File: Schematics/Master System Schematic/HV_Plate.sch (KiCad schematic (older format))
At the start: 14 parts, among them K1 AIR-: GX14, K53 PCharge: P105BDA, K54 AIR+: GX14, K55 DCharge: PNC113, U5 OrionCurrentSens

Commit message: LV Plate
> Added basic connectors and outlines for MCR PCB
> Added and wired components on LV Plate
> Added GLV connector
> Connected layers
> Some wire gauges still needed

LV_Plate Version 1.0
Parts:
- U5: symbol Master-System-Schematic-rescue:OrionCurrentSens-NER -> NER:OrionCurrentSens
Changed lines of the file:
@@
 $Descr A 11000 8500
 encoding utf-8
-Sheet 27 38
+Sheet 20 40
 Title "HV Plate"
 Date "2021-04-15"
@@
 $EndComp
 $Comp
-L Master-System-Schematic-rescue:OrionCurrentSens-NER U?
+L NER:OrionCurrentSens U?
 U 1 1 6082A419
 P 7400 5250

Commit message: Master Cleanup
> BattBox sheet tweaks
> Removed IMD container
> Removed BattBox fans from master
> Removed BMS container, temporarily moved VPM sheet
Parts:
- renumbered F204 to F?, F203 to F?, F205 to F?, F201 to F?, F202 to F?, K1 to K?, K53 to K?, K54 to K?, K55 to K?, R13 to R?, R16 to R?, R12 to R?, R11 to R?
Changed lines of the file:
@@
 $Descr A 11000 8500
 encoding utf-8
-Sheet 7 27
+Sheet 7 25
 Title "HV Plate"
 Date "2021-04-15"
@@
 $EndDescr
 $Comp
-L Device:R R11
+L Device:R R?
 U 1 1 608CF874
 P 6150 3350
-F 0 "R11" H 5750 3450 50  0000 C CNN
+F 0 "R?" H 5750 3450 50  0000 C CNN
 F 1 "PCharge: 600R" H 5750 3350 50  0000 C CNN
 F 2 "" V 6080 3350 50  0001 C CNN
@@
 $EndComp
 $Comp
-L Relay:DIPxx-1Axx-11x K1
+L Relay:DIPxx-1Axx-11x K?
 U 1 1 608D0328
 P 3450 5750
-F 0 "K1" V 2883 5750 50  0000 C CNN
+F 0 "K?" V 2883 5750 50  0000 C CNN
 F 1 "AIR-: GX14" V 2974 5750 50  0000 C CNN
 F 2 "Relay_THT:Relay_StandexMeder_DIP_LowProfile" H 3800 5700 50  0001 L CNN
@@
 $EndComp
 $Comp
-L Relay:DIPxx-1Axx-11x K54
+L Relay:DIPxx-1Axx-11x K?
 U 1 1 608D24D5
 P 4650 3750
-F 0 "K54" V 4083 3750 50  0000 C CNN
+F 0 "K?" V 4083 3750 50  0000 C CNN
 F 1 "AIR+: GX14" V 4174 3750 50  0000 C CNN
 F 2 "Relay_THT:Relay_StandexMeder_DIP_LowProfile" H 5000 3700 50  0001 L CNN
@@
 $EndComp
 $Comp
-L Device:Fuse F203
+L Device:Fuse F?
 U 1 1 608D366E
 P 2400 3950
-F 0 "F203" V 2203 3950 50  0000 C CNN
+F 0 "F?" V 2203 3950 50  0000 C CNN
 F 1 "TS Fuse: 200A" V 2294 3950 50  0000 C CNN
 F 2 "" V 2330 3950 50  0001 C CNN
@@
 $EndComp
 $Comp
-L Device:R R12
+L Device:R R?
 U 1 1 608CEF02
 P 7000 4450
-F 0 "R12" H 6650 4550 50  0000 C CNN
+F 0 "R?" H 6650 4550 50  0000 C CNN
 F 1 "DCharge: 3.3K" H 6650 4450 50  0000 C CNN
 F 2 "" V 6930 4450 50  0001 C CNN
@@
 $EndComp
 $Comp
-L Relay:MSxx-1Bxx-75 K55
+L Relay:MSxx-1Bxx-75 K?
 U 1 1 608D570D
 P 5600 5000
-F 0 "K55" V 5033 5000 50  0000 C CNN
+F 0 "K?" V 5033 5000 50  0000 C CNN
 F 1 "DCharge: PNC113" V 5124 5000 50  0000 C CNN
 F 2 "Relay_THT:Relay_SPST_StandexMeder_MS_Form1AB" H 5950 4950 50  0001 L CNN
@@
 $EndComp
 $Comp
-L Device:R R13
+L Device:R R?
 U 1 1 60827E73
 P 8950 3500
-F 0 "R13" H 8880 3454 50  0000 R CNN
+F 0 "R?" H 8880 3454 50  0000 R CNN
 F 1 "TSMP+: 10K" H 8880 3545 50  0000 R CNN
 F 2 "" V 8880 3500 50  0001 C CNN
@@
 $EndComp
 $Comp
-L Device:R R16
+L Device:R R?
 U 1 1 608282DF
 P 9050 3500
-F 0 "R16" H 8980 3454 50  0000 R CNN
+F 0 "R?" H 8980 3454 50  0000 R CNN
 F 1 "TSMP-: 10K" H 8980 3545 50  0000 R CNN
 F 2 "" V 8980 3500 50  0001 C CNN
@@
 AR Path="/5F45B05E/6082A419" Ref="U?"  Part="1"
 AR Path="/5F45B05E/6082840F/6082A419" Ref="U5"  Part="1"
-F 0 "U5" V 6950 4700 50  0000 C CNN
+F 0 "U?" V 6950 4700 50  0000 C CNN
 F 1 "OrionCurrentSens" V 6850 4700 50  0000 C CNN
 F 2 "" H 7400 5250 50  0001 C CNN
@@
 	7950 2450 7950 2800
 $Comp
-L Device:Fuse F204
+L Device:Fuse F?
 U 1 1 608289D7
 P 7850 2950
-F 0 "F204" H 7650 3050 50  0000 C CNN
+F 0 "F?" H 7650 3050 50  0000 C CNN
 F 1 "IMD Fuse+: 0.5A" H 7450 2950 50  0000 C CNN
 F 2 "" V 7780 2950 50  0001 C CNN
@@
 $EndComp
 $Comp
-L Device:Fuse F205
+L Device:Fuse F?
 U 1 1 608D8D1E
 P 7950 2950
-F 0 "F205" H 7750 3050 50  0000 C CNN
+F 0 "F?" H 7750 3050 50  0000 C CNN
 F 1 "IMD Fuse-: 0.5A" H 7550 2950 50  0000 C CNN
 F 2 "" V 7880 2950 50  0001 C CNN
@@
 PCharge_SigL
 $Comp
-L Relay:DIPxx-1Axx-11x K53
+L Relay:DIPxx-1Axx-11x K?
 U 1 1 608D1508
 P 4650 2650
-F 0 "K53" V 4083 2650 50  0000 C CNN
+F 0 "K?" V 4083 2650 50  0000 C CNN
 F 1 "PCharge: P105BDA" V 4174 2650 50  0000 C CNN
 F 2 "Relay_THT:Relay_StandexMeder_DIP_LowProfile" H 5000 2600 50  0001 L CNN
@@
 2x ??AWG
 $Comp
-L Device:Fuse F202
+L Device:Fuse F?
 U 1 1 6091E6DC
 P 1850 2950
-F 0 "F202" H 1700 3050 50  0000 C CNN
+F 0 "F?" H 1700 3050 50  0000 C CNN
 F 1 "TSAL Fuse-: ??A" H 1450 2950 50  0000 C CNN
 F 2 "" V 1780 2950 50  0001 C CNN
@@
 $EndComp
 $Comp
-L Device:Fuse F201
+L Device:Fuse F?
 U 1 1 6091E6D6
 P 1750 2950
-F 0 "F201" H 1600 3050 50  0000 C CNN
+F 0 "F?" H 1600 3050 50  0000 C CNN
 F 1 "TSAL Fuse+: ??A" H 1350 2950 50  0000 C CNN
 F 2 "" V 1680 2950 50  0001 C CNN

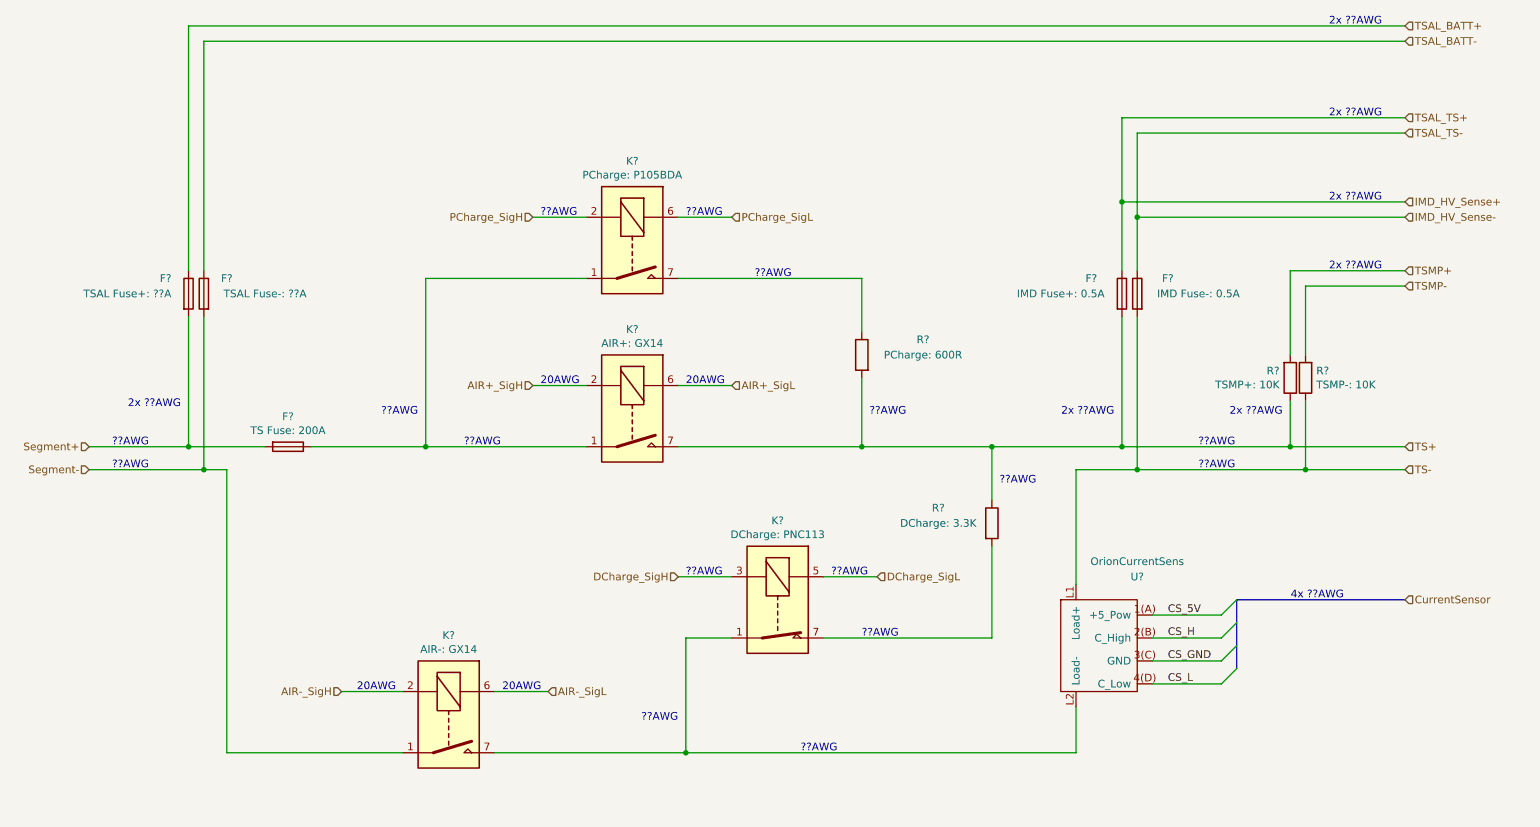
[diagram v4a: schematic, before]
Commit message: Battery Box KiCAD Update (#103)
* LV Plate and VPM board

Verified and updated LV plate connections
Setup VPM board stand-in
Organized main battery box schematic

* Battbox and master update

- Fixed all connections within battbox and did some formatting
- Added all battbox connections to master

* Annotations complete

* VPM callout

Added call to view altium schematic for VPM boarrd

* TSAL call out

Redirect to altium for TSAL

* Dates and stuff

- Final annotations
- Updated title blocks

* Exported

Plotted full file

Co-authored-by: Zack Perry <zperry2002@gmail.com>
Co-authored-by: Zack Perry <60787475+ziptol@users.noreply.github.com>
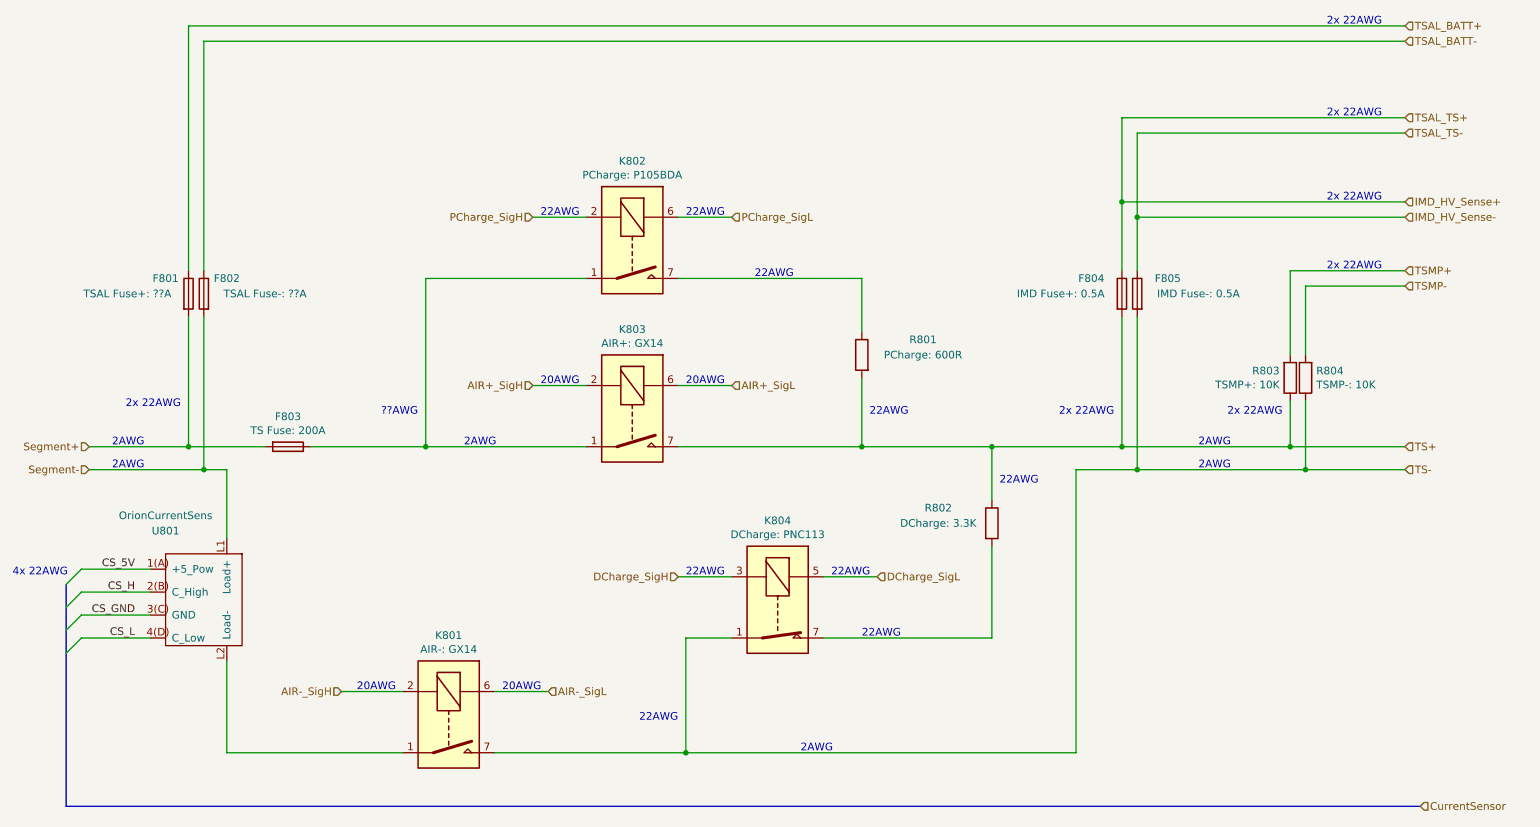
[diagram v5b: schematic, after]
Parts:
- gave numbers to parts that had none: 13
- renumbered U5 to U801
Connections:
- net Segment-: now also U801.L1 (Load+); no longer K801.1, K801.14
- net TS-: now also K801.7, K801.8, K804.1; no longer U801.L1 (Load+)
- new net: K801.1, K801.14, U801.L2 (Load-)
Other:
- note added: "22AWG"
- note added: "2AWG"
- note added: "2x 22AWG"
- note added: "4x 22AWG"
- note removed: "2x ??AWG"
- note removed: "4x ??AWG"
- moved on the sheet: U801
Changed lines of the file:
@@
 EESchema Schematic File Version 4
+LIBS:Master System Schematic-cache
 EELAYER 30 0
 EELAYER END
 $Descr A 11000 8500
 encoding utf-8
-Sheet 7 25
+Sheet 8 24
 Title "HV Plate"
 Date "2021-04-15"
 Rev "1.0"
-Comp ""
-Comment1 ""
-Comment2 ""
+Comp "Northeastern Electric Racing"
+Comment1 "https://github.com/Northeastern-Electric-Racing/NER"
+Comment2 "For authors and other info, contact Chief Electrical Engineer"
 Comment3 ""
 Comment4 ""
 $EndDescr
 $Comp
-L Device:R R?
+L Device:R R801
 U 1 1 608CF874
 P 6150 3350
-F 0 "R?" H 5750 3450 50  0000 C CNN
+F 0 "R801" H 5750 3450 50  0000 C CNN
 F 1 "PCharge: 600R" H 5750 3350 50  0000 C CNN
 F 2 "" V 6080 3350 50  0001 C CNN
@@
 $EndComp
 $Comp
-L Relay:DIPxx-1Axx-11x K?
+L Relay:DIPxx-1Axx-11x K801
 U 1 1 608D0328
 P 3450 5750
-F 0 "K?" V 2883 5750 50  0000 C CNN
+F 0 "K801" V 2883 5750 50  0000 C CNN
 F 1 "AIR-: GX14" V 2974 5750 50  0000 C CNN
 F 2 "Relay_THT:Relay_StandexMeder_DIP_LowProfile" H 3800 5700 50  0001 L CNN
@@
 $EndComp
 $Comp
-L Relay:DIPxx-1Axx-11x K?
+L Relay:DIPxx-1Axx-11x K803
 U 1 1 608D24D5
 P 4650 3750
-F 0 "K?" V 4083 3750 50  0000 C CNN
+F 0 "K803" V 4083 3750 50  0000 C CNN
 F 1 "AIR+: GX14" V 4174 3750 50  0000 C CNN
 F 2 "Relay_THT:Relay_StandexMeder_DIP_LowProfile" H 5000 3700 50  0001 L CNN
@@
 $EndComp
 $Comp
-L Device:Fuse F?
+L Device:Fuse F803
 U 1 1 608D366E
 P 2400 3950
-F 0 "F?" V 2203 3950 50  0000 C CNN
+F 0 "F803" V 2203 3950 50  0000 C CNN
 F 1 "TS Fuse: 200A" V 2294 3950 50  0000 C CNN
 F 2 "" V 2330 3950 50  0001 C CNN
@@
 $EndComp
 $Comp
-L Device:R R?
+L Device:R R802
 U 1 1 608CEF02
 P 7000 4450
-F 0 "R?" H 6650 4550 50  0000 C CNN
+F 0 "R802" H 6650 4550 50  0000 C CNN
 F 1 "DCharge: 3.3K" H 6650 4450 50  0000 C CNN
 F 2 "" V 6930 4450 50  0001 C CNN
@@
 $EndComp
 $Comp
-L Relay:MSxx-1Bxx-75 K?
+L Relay:MSxx-1Bxx-75 K804
 U 1 1 608D570D
 P 5600 5000
-F 0 "K?" V 5033 5000 50  0000 C CNN
+F 0 "K804" V 5033 5000 50  0000 C CNN
 F 1 "DCharge: PNC113" V 5124 5000 50  0000 C CNN
 F 2 "Relay_THT:Relay_SPST_StandexMeder_MS_Form1AB" H 5950 4950 50  0001 L CNN
@@
 $EndComp
 $Comp
-L Device:R R?
+L Device:R R803
 U 1 1 60827E73
 P 8950 3500
-F 0 "R?" H 8880 3454 50  0000 R CNN
+F 0 "R803" H 8880 3454 50  0000 R CNN
 F 1 "TSMP+: 10K" H 8880 3545 50  0000 R CNN
 F 2 "" V 8880 3500 50  0001 C CNN
@@
 $EndComp
 $Comp
-L Device:R R?
+L Device:R R804
 U 1 1 608282DF
 P 9050 3500
-F 0 "R?" H 8980 3454 50  0000 R CNN
+F 0 "R804" H 8980 3454 50  0000 R CNN
 F 1 "TSMP-: 10K" H 8980 3545 50  0000 R CNN
 F 2 "" V 8980 3500 50  0001 C CNN
@@
 L NER:OrionCurrentSens U?
 U 1 1 6082A419
-P 7400 5250
+P 2150 4950
 AR Path="/5F45B05E/6082A419" Ref="U?"  Part="1"
-AR Path="/5F45B05E/6082840F/6082A419" Ref="U5"  Part="1"
-F 0 "U?" V 6950 4700 50  0000 C CNN
-F 1 "OrionCurrentSens" V 6850 4700 50  0000 C CNN
-F 2 "" H 7400 5250 50  0001 C CNN
-F 3 "" H 7400 5250 50  0001 C CNN
-	1    7400 5250
-	0    -1   1    0
-$EndComp
-Text HLabel 9700 4950 2    50   Input ~ 0
+AR Path="/5F45B05E/6082840F/6082A419" Ref="U?"  Part="1"
+AR Path="/60C39CCE/6082840F/6082A419" Ref="U801"  Part="1"
+F 0 "U801" V 1700 4400 50  0000 C CNN
+F 1 "OrionCurrentSens" V 1600 4400 50  0000 C CNN
+F 2 "" H 2150 4950 50  0001 C CNN
+F 3 "" H 2150 4950 50  0001 C CNN
+	1    2150 4950
+	0    1    1    0
+$EndComp
+Text HLabel 9800 6300 2    50   Input ~ 0
 CurrentSensor
 Text HLabel 9700 3950 2    50   Input ~ 0
@@
 Segment-
 Entry Wire Line
-	8600 4950 8500 5050
+	1050 4750 950  4850
 Entry Wire Line
-	8600 5100 8500 5200
+	1050 4900 950  5000
 Entry Wire Line
-	8600 5250 8500 5350
+	1050 5050 950  5150
 Entry Wire Line
-	8600 5400 8500 5500
-Wire Wire Line
-	8500 5050 8050 5050
-Wire Wire Line
-	8500 5200 8050 5200
-Wire Wire Line
-	8500 5350 8050 5350
-Wire Wire Line
-	8500 5500 8050 5500
-Text Label 8150 5050 0    50   ~ 0
+	1050 5200 950  5300
+Wire Wire Line
+	1050 4750 1500 4750
+Wire Wire Line
+	1050 4900 1500 4900
+Wire Wire Line
+	1050 5050 1500 5050
+Wire Wire Line
+	1050 5200 1500 5200
+Text Label 1400 4750 2    50   ~ 0
 CS_5V
-Text Label 8150 5200 0    50   ~ 0
+Text Label 1400 4900 2    50   ~ 0
 CS_H
-Text Label 8150 5350 0    50   ~ 0
+Text Label 1400 5050 2    50   ~ 0
 CS_GND
-Text Label 8150 5500 0    50   ~ 0
+Text Label 1400 5200 2    50   ~ 0
 CS_L
 Text HLabel 1100 3950 0    50   Input ~ 0
@@
 Wire Wire Line
 	3750 5950 5000 5950
-Wire Wire Line
-	7550 4100 7550 4850
 Text HLabel 2750 5550 0    50   Input ~ 0
 AIR-_SigH
@@
 	5300 4800 4950 4800
 Text Notes 5000 4800 0    50   ~ 0
-??AWG
+22AWG
 Wire Wire Line
 	6250 4800 5900 4800
 Text Notes 5950 4800 0    50   ~ 0
-??AWG
+22AWG
 Wire Wire Line
 	5300 5200 5000 5200
@@
 Wire Wire Line
 	1100 4100 1850 4100
-Wire Wire Line
-	2000 4100 2000 5950
 Text HLabel 9700 2900 2    50   Input ~ 0
 TSMP-
@@
 IMD_HV_Sense+
 Wire Wire Line
-	7550 5650 7550 5950
-Wire Bus Line
-	9700 4950 8600 4950
-Wire Wire Line
 	7950 2450 7950 2800
 $Comp
-L Device:Fuse F?
+L Device:Fuse F804
 U 1 1 608289D7
 P 7850 2950
-F 0 "F?" H 7650 3050 50  0000 C CNN
+F 0 "F804" H 7650 3050 50  0000 C CNN
 F 1 "IMD Fuse+: 0.5A" H 7450 2950 50  0000 C CNN
 F 2 "" V 7780 2950 50  0001 C CNN
@@
 $EndComp
 $Comp
-L Device:Fuse F?
+L Device:Fuse F805
 U 1 1 608D8D1E
 P 7950 2950
-F 0 "F?" H 7750 3050 50  0000 C CNN
+F 0 "F805" H 7750 3050 50  0000 C CNN
 F 1 "IMD Fuse-: 0.5A" H 7550 2950 50  0000 C CNN
 F 2 "" V 7880 2950 50  0001 C CNN
@@
 	7950 2450 9700 2450
 Text Notes 5000 2450 0    50   ~ 0
-??AWG
+22AWG
 Text Notes 4050 2450 0    50   ~ 0
-??AWG
+22AWG
 Wire Wire Line
 	5300 2450 4950 2450
@@
 PCharge_SigL
 $Comp
-L Relay:DIPxx-1Axx-11x K?
+L Relay:DIPxx-1Axx-11x K802
 U 1 1 608D1508
 P 4650 2650
-F 0 "K?" V 4083 2650 50  0000 C CNN
+F 0 "K802" V 4083 2650 50  0000 C CNN
 F 1 "PCharge: P105BDA" V 4174 2650 50  0000 C CNN
 F 2 "Relay_THT:Relay_StandexMeder_DIP_LowProfile" H 5000 2600 50  0001 L CNN
@@
 $EndComp
 Text Notes 8350 3950 0    50   ~ 0
-??AWG
+2AWG
 Text Notes 3550 3950 0    50   ~ 0
-??AWG
+2AWG
 Text Notes 1250 4100 0    50   ~ 0
-??AWG
+2AWG
 Text Notes 5750 5950 0    50   ~ 0
-??AWG
+2AWG
 Text Notes 8350 4100 0    50   ~ 0
-??AWG
+2AWG
 Text Notes 7800 3750 2    50   ~ 0
-2x ??AWG
+2x 22AWG
 Text Notes 8900 3750 2    50   ~ 0
-2x ??AWG
-Text Notes 9300 4950 2    50   ~ 0
-4x ??AWG
+2x 22AWG
+Text Notes 600  4800 0    50   ~ 0
+4x 22AWG
 Text Notes 9550 2350 2    50   ~ 0
-2x ??AWG
+2x 22AWG
 Text Notes 9550 2800 2    50   ~ 0
-2x ??AWG
+2x 22AWG
 Text Notes 3250 3750 2    50   ~ 0
 ??AWG
 Text Notes 5450 2850 0    50   ~ 0
-??AWG
+22AWG
 Text Notes 6200 3750 0    50   ~ 0
-??AWG
+22AWG
 Wire Wire Line
 	3300 2850 4350 2850
@@
 	2550 3950 3300 3950
 Text Notes 1250 3950 0    50   ~ 0
-??AWG
+2AWG
 Text Notes 7050 4200 0    50   ~ 0
-??AWG
+22AWG
 Text Notes 6150 5200 0    50   ~ 0
-??AWG
+22AWG
 Text Notes 4950 5750 2    50   ~ 0
-??AWG
+22AWG
 Text HLabel 9700 1800 2    50   Input ~ 0
 TSAL_TS+
@@
 	9700 1900 7950 1900
 Text Notes 9550 1800 2    50   ~ 0
-2x ??AWG
+2x 22AWG
 Text Notes 9550 1200 2    50   ~ 0
-2x ??AWG
-$Comp
-L Device:Fuse F?
+2x 22AWG
+$Comp
+L Device:Fuse F802
 U 1 1 6091E6DC
 P 1850 2950
-F 0 "F?" H 1700 3050 50  0000 C CNN
+F 0 "F802" H 1700 3050 50  0000 C CNN
 F 1 "TSAL Fuse-: ??A" H 1450 2950 50  0000 C CNN
 F 2 "" V 1780 2950 50  0001 C CNN
@@
 $EndComp
 $Comp
-L Device:Fuse F?
+L Device:Fuse F801
 U 1 1 6091E6D6
 P 1750 2950
-F 0 "F?" H 1600 3050 50  0000 C CNN
+F 0 "F801" H 1600 3050 50  0000 C CNN
 F 1 "TSAL Fuse+: ??A" H 1350 2950 50  0000 C CNN
 F 2 "" V 1680 2950 50  0001 C CNN
@@
 	1850 1300 1850 2800
 Text Notes 1700 3700 2    50   ~ 0
-2x ??AWG
+2x 22AWG
 Wire Wire Line
 	7850 2350 9700 2350
@@
 Connection ~ 7950 2450
 Wire Bus Line
-	8600 4950 8600 5400
+	950  6300 9800 6300
+Wire Wire Line
+	2000 4100 2000 4550
+Wire Wire Line
+	2000 5350 2000 5950
+Wire Wire Line
+	7550 4100 7550 5950
+Wire Bus Line
+	950  4850 950  6300
 $EndSCHEMATC
